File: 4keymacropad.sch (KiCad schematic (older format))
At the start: 5 parts, among them J1 Conn_01x05, SW1 SW_Push, SW2 SW_Push, SW3 SW_Push, SW4 SW_Push

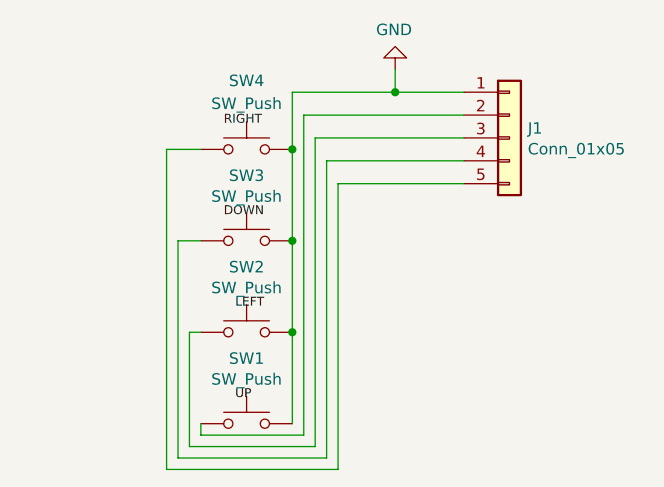
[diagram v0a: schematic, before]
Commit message: Updates to use rows/columns from mainboard
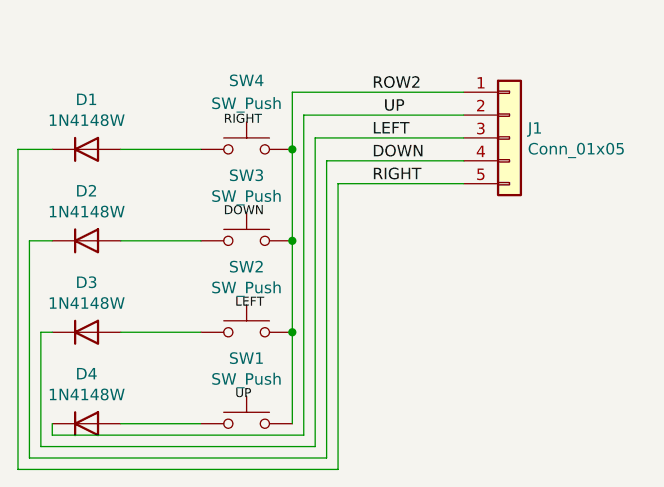
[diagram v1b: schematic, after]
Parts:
- added D1, D2, D3, D4: 1N4148W, Diode_SMD:D_SOD-123, symbol Diode:1N4148W
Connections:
- net DOWN: now also J1.4 (Pin_4), D2.1 (K)
- net LEFT: now also J1.3 (Pin_3), D3.1 (K)
- net RIGHT: now also J1.5 (Pin_5), D1.1 (K)
- net UP: now also J1.2 (Pin_2), D4.1 (K)
- net at SW1.1: now also D4.2 (A); no longer J1.2 (Pin_2)
- net at SW3.1: now also D2.2 (A); no longer J1.4 (Pin_4)
- net at SW2.1: now also D3.2 (A); no longer J1.3 (Pin_3)
- net at SW4.1: now also D1.2 (A); no longer J1.5 (Pin_5)
- net GND renamed ROW2
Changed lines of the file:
@@
 	1    0    0    -1
 $EndComp
-Wire Wire Line
-	5600 3350 5450 3350
 Text Label 5700 3250 0    39   ~ 0
 RIGHT
@@
 Text Label 5750 4050 0    39   ~ 0
 LEFT
-Wire Wire Line
-	5600 4150 5550 4150
 $Comp
 L Switch:SW_Push SW2
@@
 Text Label 5700 3650 0    39   ~ 0
 DOWN
-Wire Wire Line
-	5600 3750 5500 3750
 $Comp
 L Switch:SW_Push SW3
@@
 	6000 3750 6000 3350
 Wire Wire Line
-	5600 4550 5600 4600
-Wire Wire Line
-	5600 4600 6050 4600
-Wire Wire Line
-	5550 4150 5550 4650
-Wire Wire Line
-	5500 3750 5500 4700
-Wire Wire Line
-	5450 3350 5450 4750
-Wire Wire Line
-	5500 4700 6150 4700
-Wire Wire Line
-	5550 4650 6100 4650
-Wire Wire Line
-	5450 4750 6200 4750
-Wire Wire Line
 	6050 4600 6050 3200
 Wire Wire Line
@@
 	6050 3200 6750 3200
 $Comp
-L power:GND #PWR0101
-U 1 1 61CE6B0B
-P 6450 3000
-F 0 "#PWR0101" H 6450 2750 50  0001 C CNN
-F 1 "GND" H 6455 2827 50  0000 C CNN
-F 2 "" H 6450 3000 50  0001 C CNN
-F 3 "" H 6450 3000 50  0001 C CNN
-	1    6450 3000
-	-1   0    0    1
+L Diode:1N4148W D1
+U 1 1 61D3073C
+P 5100 3350
+F 0 "D1" H 5100 3567 50  0000 C CNN
+F 1 "1N4148W" H 5100 3476 50  0000 C CNN
+F 2 "Diode_SMD:D_SOD-123" H 5100 3175 50  0001 C CNN
+F 3 "https://www.vishay.com/docs/85748/1n4148w.pdf" H 5100 3350 50  0001 C CNN
+	1    5100 3350
+	1    0    0    -1
+$EndComp
+$Comp
+L Diode:1N4148W D4
+U 1 1 61D33160
+P 5100 4550
+F 0 "D4" H 5100 4767 50  0000 C CNN
+F 1 "1N4148W" H 5100 4676 50  0000 C CNN
+F 2 "Diode_SMD:D_SOD-123" H 5100 4375 50  0001 C CNN
+F 3 "https://www.vishay.com/docs/85748/1n4148w.pdf" H 5100 4550 50  0001 C CNN
+	1    5100 4550
+	1    0    0    -1
+$EndComp
+$Comp
+L Diode:1N4148W D2
+U 1 1 61D315CE
+P 5100 3750
+F 0 "D2" H 5100 3967 50  0000 C CNN
+F 1 "1N4148W" H 5100 3876 50  0000 C CNN
+F 2 "Diode_SMD:D_SOD-123" H 5100 3575 50  0001 C CNN
+F 3 "https://www.vishay.com/docs/85748/1n4148w.pdf" H 5100 3750 50  0001 C CNN
+	1    5100 3750
+	1    0    0    -1
+$EndComp
+$Comp
+L Diode:1N4148W D3
+U 1 1 61D3BDE5
+P 5100 4150
+F 0 "D3" H 5100 4367 50  0000 C CNN
+F 1 "1N4148W" H 5100 4276 50  0000 C CNN
+F 2 "Diode_SMD:D_SOD-123" H 5100 3975 50  0001 C CNN
+F 3 "https://www.vishay.com/docs/85748/1n4148w.pdf" H 5100 4150 50  0001 C CNN
+	1    5100 4150
+	1    0    0    -1
 $EndComp
 Wire Wire Line
-	6450 3000 6450 3100
+	5250 3350 5600 3350
 Wire Wire Line
-	6000 3100 6450 3100
+	5250 3750 5600 3750
 Wire Wire Line
-	6450 3100 6750 3100
-Connection ~ 6450 3100
+	5250 4150 5600 4150
+Wire Wire Line
+	5600 4550 5250 4550
+Wire Wire Line
+	4950 4550 4950 4600
+Wire Wire Line
+	4950 4600 6050 4600
+Wire Wire Line
+	4950 4150 4900 4150
+Wire Wire Line
+	4900 4150 4900 4650
+Wire Wire Line
+	4900 4650 6100 4650
+Wire Wire Line
+	4950 3750 4850 3750
+Wire Wire Line
+	4850 3750 4850 4700
+Wire Wire Line
+	4850 4700 6150 4700
+Wire Wire Line
+	4950 3350 4800 3350
+Wire Wire Line
+	4800 3350 4800 4750
+Wire Wire Line
+	4800 4750 6200 4750
+Wire Wire Line
+	6000 3100 6750 3100
+Text Label 6350 3100 0    50   ~ 0
+ROW2
+Text Label 6400 3200 0    50   ~ 0
+UP
+Text Label 6350 3300 0    50   ~ 0
+LEFT
+Text Label 6350 3400 0    50   ~ 0
+DOWN
+Text Label 6350 3500 0    50   ~ 0
+RIGHT
 $EndSCHEMATC
